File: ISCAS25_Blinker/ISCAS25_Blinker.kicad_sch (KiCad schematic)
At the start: 6 parts, among them Q1 BC846, U1 LMC555xM

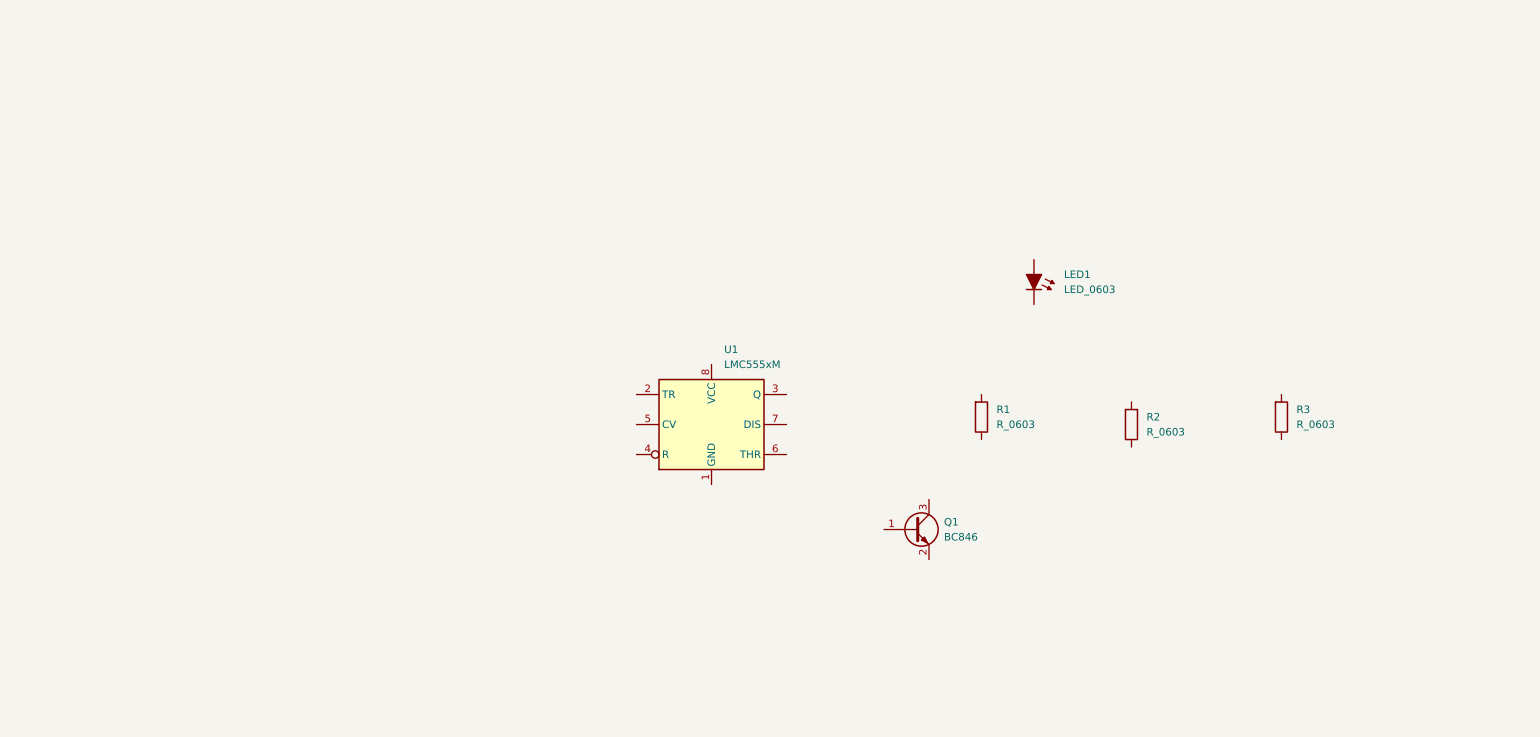
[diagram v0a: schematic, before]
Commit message: Schematic done
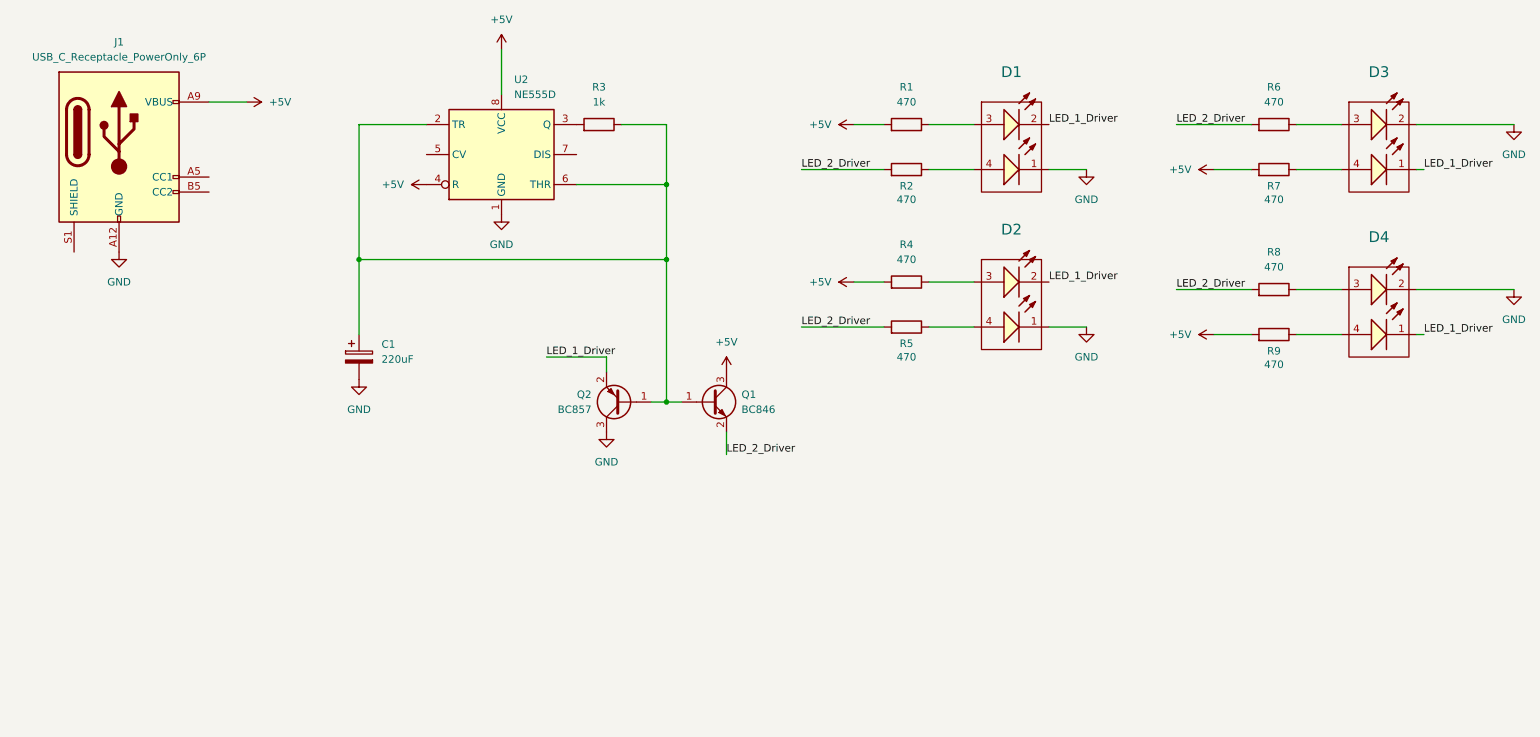
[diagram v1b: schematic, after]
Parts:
- removed LED1: LED_0603, PCM_LED_SMD_AKL:LED_0603_1608Metric, symbol PCM_LED_AKL:LED_0603
- removed U1: LMC555xM, Package_SO:SOIC-8_3.9x4.9mm_P1.27mm, symbol Timer:LMC555xM
- added C1: 220uF, Capacitor_THT:C_Rect_L11.0mm_W6.4mm_P10.00mm_MKT, symbol PCM_Capacitor_AKL:CP_Radial_D6.3mm_P2.50mm
- added D1, D2, D3, D4: Red & Blue, 120°, WL-SBRW_1205_reverse mount, symbol Library:156125RB73000
- added J1: USB_C_Receptacle_PowerOnly_6P, Connector_USB:USB_C_Receptacle_GCT_USB4125-xx-x-0190_6P_TopMnt_Horizontal, symbol Connector:USB_C_Receptacle_PowerOnly_6P
- added Q2: BC857, Package_TO_SOT_SMD:SOT-23, symbol Transistor_BJT:BC857
- added R4, R5, R6, R7, R8, R9: 470, PCM_Resistor_SMD_AKL:R_0603_1608Metric, symbol PCM_Resistor_AKL:R_0603
- added U2: NE555D, Package_SO:SOIC-8_3.9x4.9mm_P1.27mm, symbol Timer:NE555D
- R1, R2: value R_0603 -> 470
- R3: value R_0603 -> 1k
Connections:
- net at R3.1: now also U2.3 (Q)
- net at R3.2: now also Q1.1 (B), C1.1, Q2.1 (B), U2.2 (TR), U2.6 (THR)
- net +5V: now reaches R1.1
- net +5V: now also Q1.3 (C), J1.A9 (VBUS), J1.B9 (VBUS), R4.1, R7.1, R9.1, U2.4 (R), U2.8 (VCC)
- net at R1.2: now also D1.3 (A)
- net LED_2_Driver: now reaches Q1.2 (E)
- net LED_2_Driver: now also R2.1, R5.1, R6.1, R8.1
- net at R2.2: now also D1.4 (A)
- new net: D2.3 (A), R4.2
- new net: D4.3 (A), R8.2
- new net: D4.4 (A), R9.2
- new net: D3.3 (A), R6.2
- new net: D2.4 (A), R5.2
- new net: D3.4 (A), R7.2
- new net GND: C1.2, D1.1 (K), D2.1 (K), D3.2 (K), D4.2 (K), J1.A12 (GND), J1.B12 (GND), Q2.3 (C), U2.1 (GND)
- new net LED_1_Driver: D1.2 (K), D2.2 (K), D3.1 (K), D4.1 (K), Q2.2 (E)
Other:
- company: (none) -> ATC US
- title: (none) -> ISCAS25_Blinker
- moved on the sheet: Q1, R1, R2, R3

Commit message: Finished but not panelized
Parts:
- added C2: 0.1uF, Capacitor_SMD:C_0603_1608Metric, symbol Device:C
- added S1: SLW-1277545-3A-RA-N-D, Library:SW_SLW-1277545-3A-RA-N-D, symbol Library:SLW-1277545-3A-RA-N-D
- C1: footprint Capacitor_THT:C_Rect_L11.0mm_W6.4mm_P10.00mm_MKT -> Capacitor_THT:CP_Radial_D6.3mm_P2.50mm
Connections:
- net +5V: now also C2.1, S1.1; no longer J1.A9 (VBUS), J1.B9 (VBUS)
- net GND: now also C2.2
- new net: J1.A9 (VBUS), J1.B9 (VBUS), S1.2
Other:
- moved on the sheet: C1, D1, D2, D3, D4, J1, Q1, Q2, R1, R2, R3, R4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

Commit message: Changes in BOM information
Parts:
- C1: Manufacturer (none) -> Panasonic; Manufacturer Part Number (none) -> ECE-A0JKA221
- C2: Manufacturer (none) -> Murata; Manufacturer Part Number (none) -> GCJ188R71C104MA01D
- J1: Manufacturer (none) -> Same Sky; Manufacturer Part Number (none) -> UJC-H-G-SMT-P6-TR
- Q1: Manufacturer (none) -> Nexperia; Manufacturer Part Number (none) -> BC846-QR
- Q2: Manufacturer (none) -> Nexperia; Manufacturer Part Number (none) -> BC857-QR
- R1, R2, R4, R5, R6, R7, R8, R9: Manufacturer (none) -> Yageo; Manufacturer Part Number (none) -> AC0603FR-7W470RL
- R3: Manufacturer (none) -> Yageo; Manufacturer Part Number (none) -> AC0603FR-7W1KL
- S1: Manufacturer (none) -> Same Sky; Manufacturer Part Number (none) -> SLW-1277545-3A-RA-N-D
- U2: Manufacturer (none) -> Texas Instruments; Manufacturer Part Number (none) -> NE555DR
